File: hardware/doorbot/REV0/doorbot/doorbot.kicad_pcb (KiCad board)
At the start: 2 copper layers, 35 parts, among them J1 Raspberry_Pi_2_3, J2 Screw_Terminal_01x12, J3 PoE, Q1 2N7002, U1 ATmega328P-AU, U2 TLP291, U3 TLP291, U4 TLP291, U5 TLP291, U6 TLP291, U7 DRV103, U8 L78L05_SO8

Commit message: more doorbot schematic & pcb work
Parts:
- added R19: 47, Resistors_SMD:R_0603, B.Cu at (131.4, 71.1)
- added R20: 47, Resistors_SMD:R_0603, B.Cu at (128.3, 71.1)
- added R21: 47, Resistors_SMD:R_0603, B.Cu at (134.6, 71.1)
- added R22: 47, Resistors_SMD:R_0603, B.Cu at (153.0, 71.1)
- C2: footprint C_0201_0603Metric -> Capacitors_SMD:CP_Elec_3x5.3
- J3: value PoE -> PoE Passthrough
- R1, R10, R11, R12, R13, R14, R15, R16, R18, R2, R3, R5, R6, R7, R8, R9: footprint Resistor_SMD:R_0603_1608Metric -> Resistors_SMD:R_0603
- R17: value R_Small_US -> 100; footprint Resistor_SMD:R_0603_1608Metric -> Resistors_SMD:R_0603
- R4: value 10 -> 47; footprint Resistor_SMD:R_0603_1608Metric -> Resistors_SMD:R_0603
- U8: value L78L05_SO8 -> MC78L05_SOT89; footprint Package_SO:SOIC-8_3.9x4.9mm_P1.27mm -> TO_SOT_Packages_SMD:SOT-89-3_Handsoldering
- moved R4 38.8 mm to (117.5, 71.1)
- moved R6 38.7 mm to (114.3, 71.1)
- moved C3 35.7 mm to (164.5, 76.8)
- moved U8 28.6 mm to (165.1, 85.1), turned to 0 degrees
- moved C4 24.3 mm to (164.5, 89.5)
- moved R12 19.4 mm to (135.9, 92.1)
- moved C2 18.5 mm to (164.5, 80.0)
- moved R5 16.1 mm to (139.1, 71.1)
- moved U6 16.0 mm to (132.7, 95.2)
- moved D1 14.4 mm to (149.9, 102.2), turned to 0 degrees
- moved R7 13.8 mm to (152.4, 85.1), turned to 90 degrees
- moved R8 13.1 mm to (154.3, 85.1)
- moved R17 13.0 mm to (132.7, 101.6)
- moved U4 12.7 mm to (123.8, 95.2)
- moved Q1 10.7 mm to (151.1, 88.9), turned to 90 degrees
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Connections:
- net Net-(J2-Pad5) renamed /WG_D0_RAW
- net Net-(J2-Pad6) renamed /WG_D1_RAW
- J1 pad 12: Net-(J1-Pad12) -> /ICSP_MISO
- J1 pad 16: Net-(J1-Pad16) -> /ICSP_MOSI
- J1 pad 18: Net-(J1-Pad18) -> /ICSP_SCK
- J1 pad 32: Net-(J1-Pad32) -> /ICSP_RESET
- R4 pad 2: Net-(J1-Pad33) -> Net-(J1-Pad5)
- R6 pad 2: Net-(J1-Pad32) -> Net-(J1-Pad3)
- U1 pad 15: Net-(U1-Pad15) -> /AT_MOSI
- U1 pad 16: Net-(U1-Pad16) -> /AT_MISO
- U1 pad 17: Net-(U1-Pad17) -> /AT_SCK
- U1 pad 29: Net-(U1-Pad29) -> /AT_RST
- U8 pad 3: Earth -> +12VA
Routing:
- net /WG_D0: track 22.1 -> 0.00 mm, vias 2 -> 0
- net /WG_D1: track 19.7 -> 0.00 mm, vias 2 -> 0
- net Net-(Q1-Pad3): track 0.00 -> 18.2 mm, vias 0 -> 2
- net Net-(U3-Pad2): track 0.00 -> 17.3 mm, vias 0 -> 2
- net +12VA: track 0.00 -> 17.1 mm, vias 0 -> 1
- net /SOLENOID_LOW: track 0.00 -> 11.1 mm, vias 0 -> 1
- net Net-(R13-Pad1): track 0.00 -> 11.1 mm
- net Net-(C1-Pad1): track 0.00 -> 8.79 mm
- net Net-(R14-Pad1): track 0.00 -> 7.15 mm
- net /AT_RXD: track 5.62 -> 0.00 mm
- net /AT_TXD: track 5.35 -> 0.00 mm
- net Net-(Q1-Pad1): track 0.00 -> 4.94 mm
- net Net-(R7-Pad2): track 0.00 -> 4.47 mm
- net +5VA: track 0.00 -> 3.35 mm
- net Net-(R9-Pad2): track 0.00 -> 2.15 mm
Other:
- board text added: "PWR.12V"
- board text added: "PWR.GND"
- board text added: "RFID.12V"
- board text added: "RFID.D0"
- board text added: "RFID.D1"
- board text added: "RFID.GND"
- board text added: "SOL.A"
- board text added: "SOL.B"
- board text added: "SW.A"
- board text added: "SW.B"

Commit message: moar doorbot pcb
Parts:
- added R23: 47, Resistor_SMD:R_0603_1608Metric, B.Cu at (118.9, 91.9)
- R1, R10, R11, R12, R13, R14, R15, R16, R17, R18, R19, R2, R20, R21, R22, R3, R4, R5, R6, R7, R8, R9: footprint Resistors_SMD:R_0603 -> Resistor_SMD:R_0603_1608Metric
- moved R11 17.7 mm to (137.2, 79.5), turned to 180 degrees
- moved R12 10.9 mm to (137.2, 81.2), turned to 180 degrees
- moved R17 0.99 mm to (133.5, 101.0)
- moved R16 0.61 mm to (129.0, 101.0)
- moved R18 0.60 mm to (124.5, 101.0)
- moved R10 0.13 mm to (120.7, 91.9)
- turned R19 to 270 degrees
- turned R20 to 270 degrees
- turned R21 to 270 degrees
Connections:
- R4 pad 2: Net-(J1-Pad5) -> Net-(J1-Pad29)
- R6 pad 2: Net-(J1-Pad3) -> Net-(J1-Pad7)
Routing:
- net +5VA: track 3.35 -> 63.1 mm, vias 0 -> 4
- net +3V3: track 0.00 -> 58.9 mm, vias 0 -> 2
- net +5V: track 0.00 -> 58.2 mm, vias 0 -> 1
- net Net-(J1-Pad31): track 0.00 -> 54.9 mm, vias 0 -> 2
- net Net-(R4-Pad1): track 0.00 -> 54.3 mm, vias 0 -> 4
- net Net-(R6-Pad1): track 0.00 -> 47.7 mm
- net Net-(J1-Pad29): track 0.00 -> 46.8 mm, vias 0 -> 3
- net +12VA: track 17.1 -> 58.7 mm, vias 1 -> 5
- net /AT_RST: track 0.00 -> 37.2 mm, vias 0 -> 2
- net /WG_D0: track 0.00 -> 30.6 mm, vias 0 -> 2
- net /AT_MOSI: track 0.00 -> 25.2 mm, vias 0 -> 2
- net /AT_SCK: track 0.00 -> 23.1 mm, vias 0 -> 2
- net /AT_MISO: track 0.00 -> 20.9 mm, vias 0 -> 2
- net Earth: track 0.00 -> 17.0 mm, vias 0 -> 6
- net /WG_D1: track 0.00 -> 17.0 mm, vias 0 -> 2
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- added copper zone on B.Cu, net Earth
- added copper zone on B.Cu, net GND
- added copper zone on F.Cu, net GND

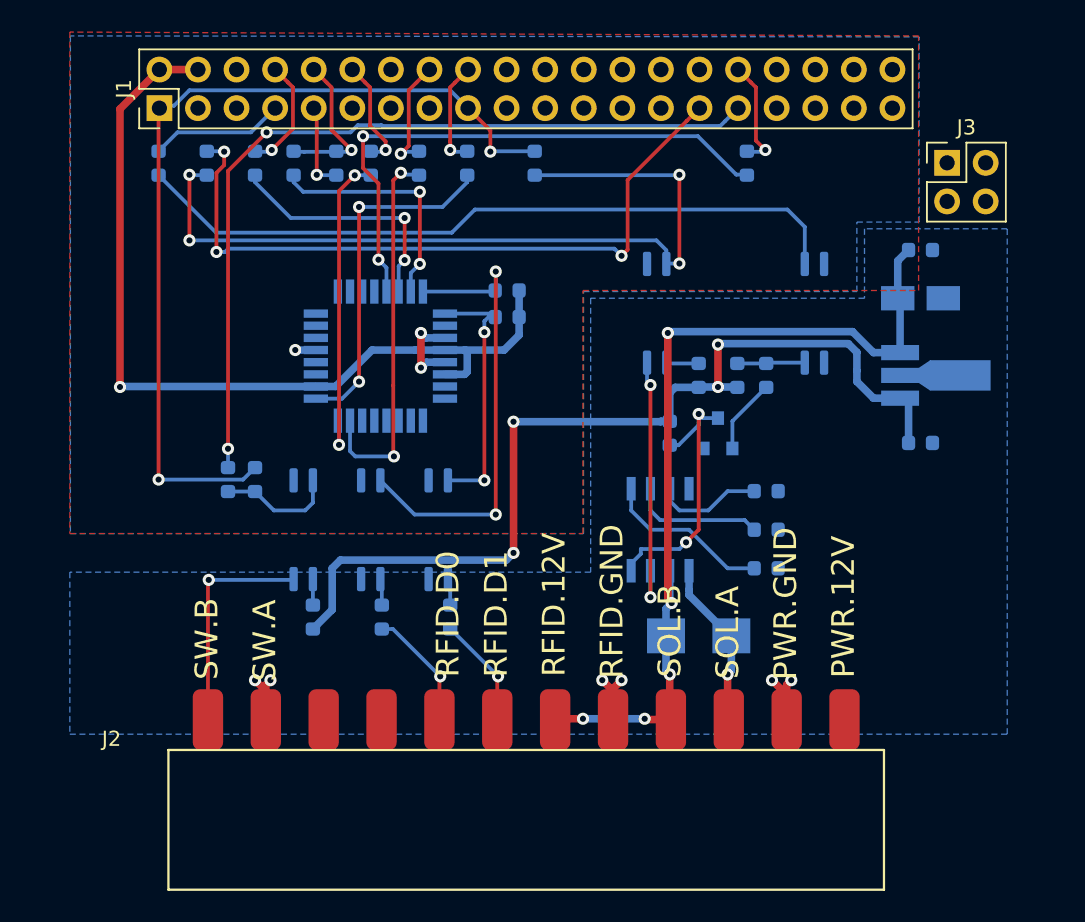
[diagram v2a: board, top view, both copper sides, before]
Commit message: doorbot: add dc boost for 24v option, PTC fuse
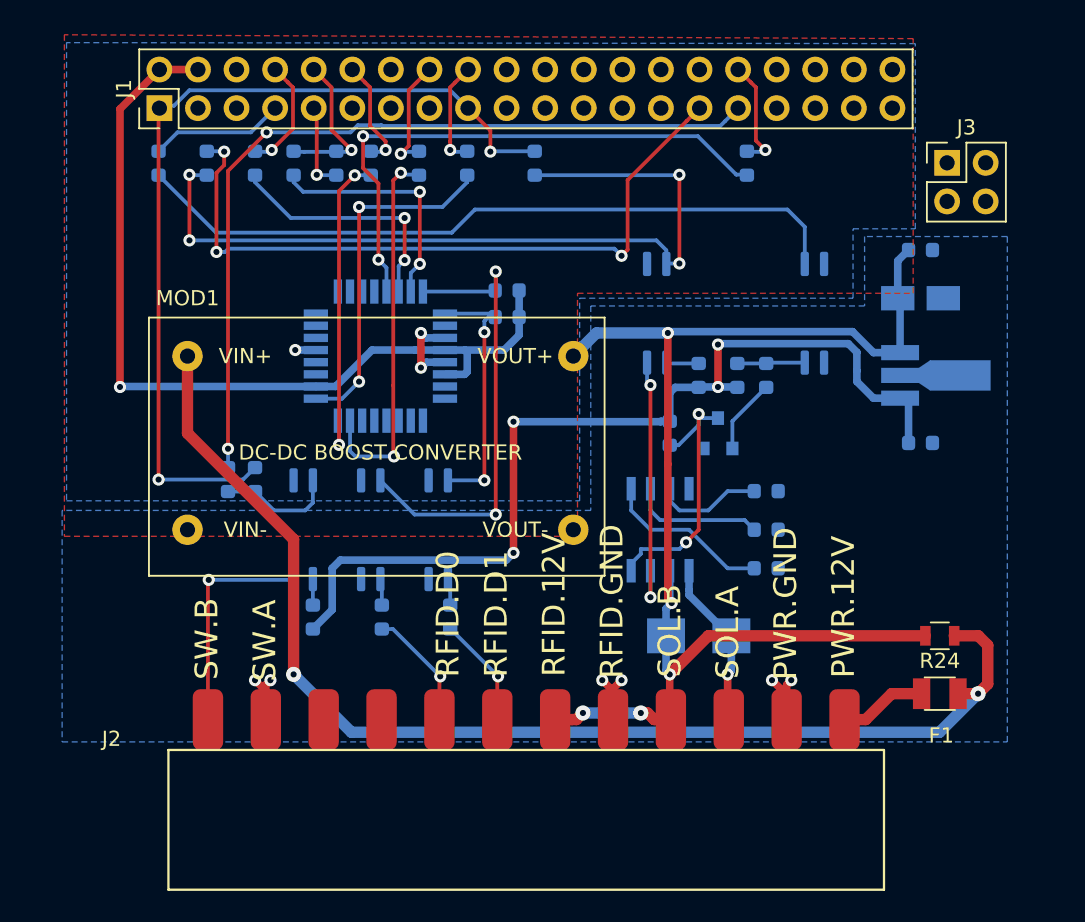
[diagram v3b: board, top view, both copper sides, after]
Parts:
- added F1: 1.5A PTC, Fuse_Holders_and_Fuses:Fuse_SMD1206_Reflow, F.Cu at (165.7, 106.0)
- added MOD1: DC_BOOST_MODULE, doorbot_pcb_library:DC_BOOST_MODULE, F.Cu at (113.7, 81.3)
- added R24: 0, Resistors_SMD:R_0805, F.Cu at (165.7, 102.2)
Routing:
- net Net-(F1-Pad1): track 0.00 -> 78.9 mm, vias 0 -> 2
- net +12VA: track 58.7 -> 83.8 mm
- net /+12V_IN: track 0.00 -> 5.78 mm

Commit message: more doorbot schematic & pcb, routed and passes drc but not complete
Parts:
- added C5: .1uF, Capacitor_SMD:C_0603_1608Metric, B.Cu at (135.6, 84.3)
- added C6: .1uF, Capacitor_SMD:C_0603_1608Metric, B.Cu at (121.9, 85.1)
- added REF**: MountingHole_2.7mm_M2.5_ISO14580, MountingHole:MountingHole_2.7mm_M2.5_ISO14580, F.Cu at (128.0, 117.1)
- added REF**: MountingHole_2.7mm_M2.5_ISO14580, MountingHole:MountingHole_2.7mm_M2.5_ISO14580, F.Cu at (182.9, 114.8)
- added REF**: MountingHole_2.7mm_M2.5_ISO14580, MountingHole:MountingHole_2.7mm_M2.5_ISO14580, F.Cu at (108.7, 63.5)
- added REF**: MountingHole_2.7mm_M2.5_ISO14580, MountingHole:MountingHole_2.7mm_M2.5_ISO14580, F.Cu at (176.5, 65.5)
- moved C2 31.1 mm to (140.7, 100.1), turned to 180 degrees
- moved C3 4.19 mm to (164.6, 81.0)
- moved R18 0.60 mm to (124.5, 101.6)
- moved R16 0.57 mm to (129.0, 101.6)
- moved R17 0.57 mm to (133.5, 101.6)
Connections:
- C2 pad 1: +12VA -> +VSW
- D1 pad 1: +12VA -> +VSW
- F1 pad 1: Net-(F1-Pad1) -> +12VA
- J2 pad 9: +12VA -> +VSW
- MOD1 pad 1: Net-(F1-Pad1) -> +12VA
- MOD1 pad 3: +12VA -> +VSW
- R24 pad 1: Net-(F1-Pad1) -> +12VA
- R24 pad 2: +12VA -> +VSW
- U7 pad 6: +12VA -> +VSW
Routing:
- net Net-(F1-Pad1): track 78.9 -> 0.00 mm, vias 2 -> 0
- net +VSW: track 0.00 -> 52.3 mm, vias 0 -> 2
- net GND: track 12.9 -> 51.1 mm, vias 4 -> 5
- net +12VA: track 83.8 -> 112.5 mm, vias 5 -> 4
- net +5V: track 58.2 -> 52.4 mm
- net /DOOR_SWITCH_IN: track 14.8 -> 12.5 mm
- net /AT_RST: track 37.2 -> 38.2 mm
- net /PI_RXD: track 10.2 -> 11.0 mm
- net Net-(R18-Pad1): track 1.75 -> 2.31 mm
- net Net-(R16-Pad2): track 1.79 -> 2.33 mm
- net Net-(R17-Pad2): track 1.81 -> 2.35 mm
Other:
- board text added: "R.12V"
- board text added: "R.D0"
- board text added: "R.D1"
- board text added: "R.GND"
- board text removed: "RFID.12V"
- board text removed: "RFID.D0"
- board text removed: "RFID.D1"
- board text removed: "RFID.GND"

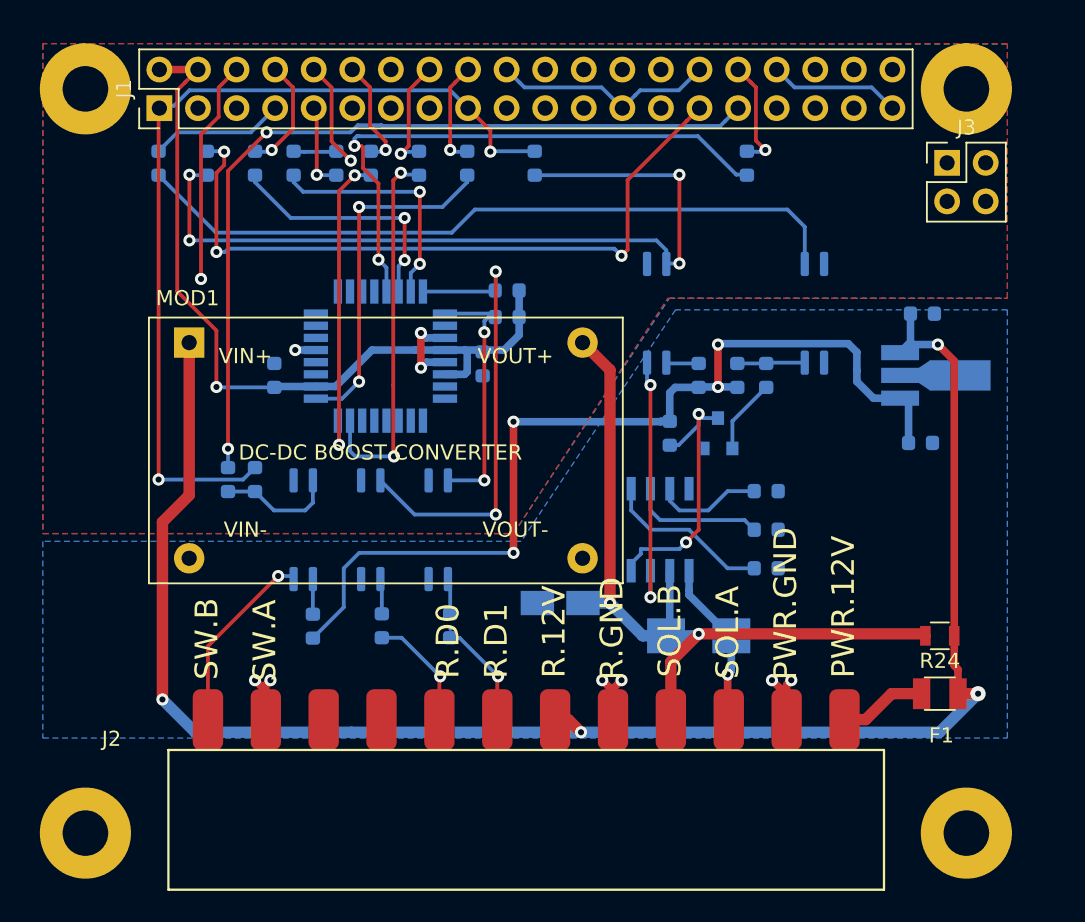
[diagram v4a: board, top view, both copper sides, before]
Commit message: add a couple 3d models
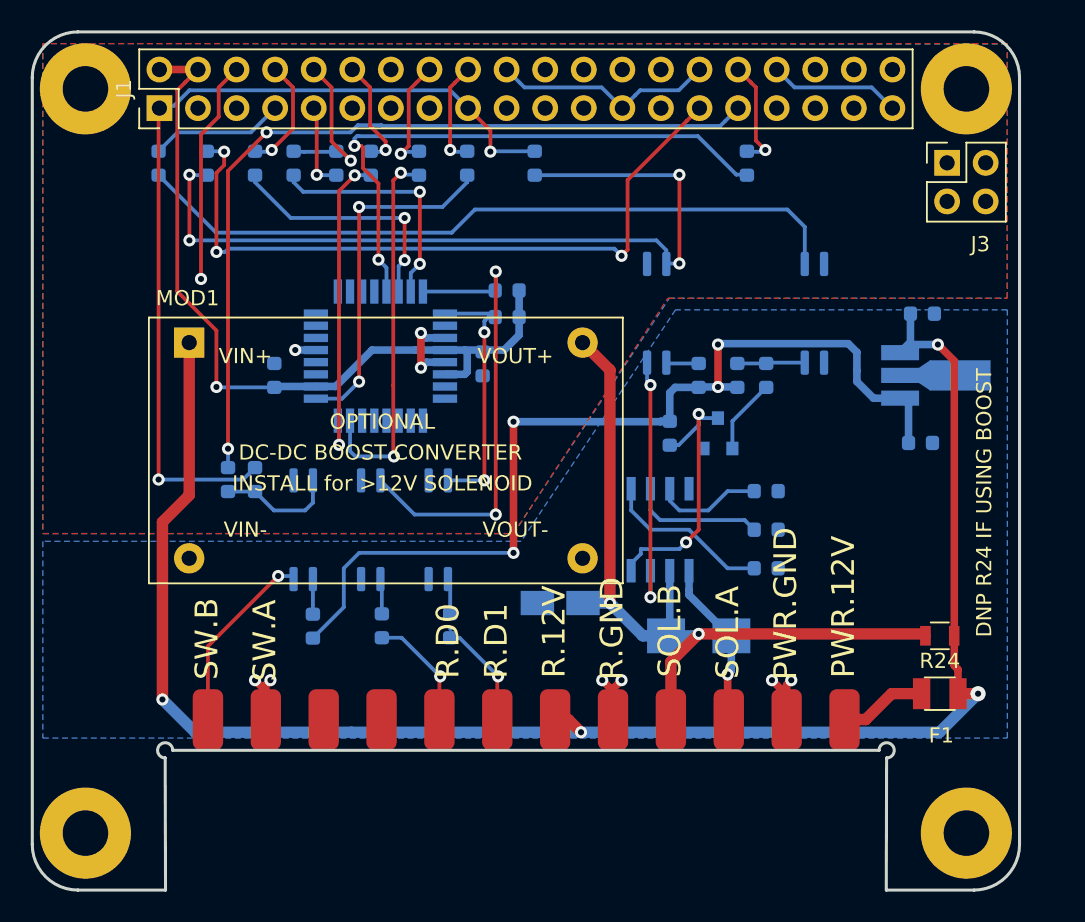
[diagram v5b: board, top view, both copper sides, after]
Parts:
- J1: footprint Connector_PinHeader_2.54mm:PinHeader_2x20_P2.54mm_Vertical -> doorbot_pcb_library:PinHeader_2x20_P2.54mm_Vertical
- J3: footprint Connector_PinHeader_2.54mm:PinHeader_2x02_P2.54mm_Vertical -> doorbot_pcb_library:PinHeader_2x02_P2.54mm_Vertical
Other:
- board outline added: 65 x 56.5 mm
- board text added: "DNP R24 IF USING BOOST"
- board text added: "INSTALL for >12V SOLENOID"
- board text added: "OPTIONAL"

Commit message: add wiegand led/buzzer control, leds, some rerouting
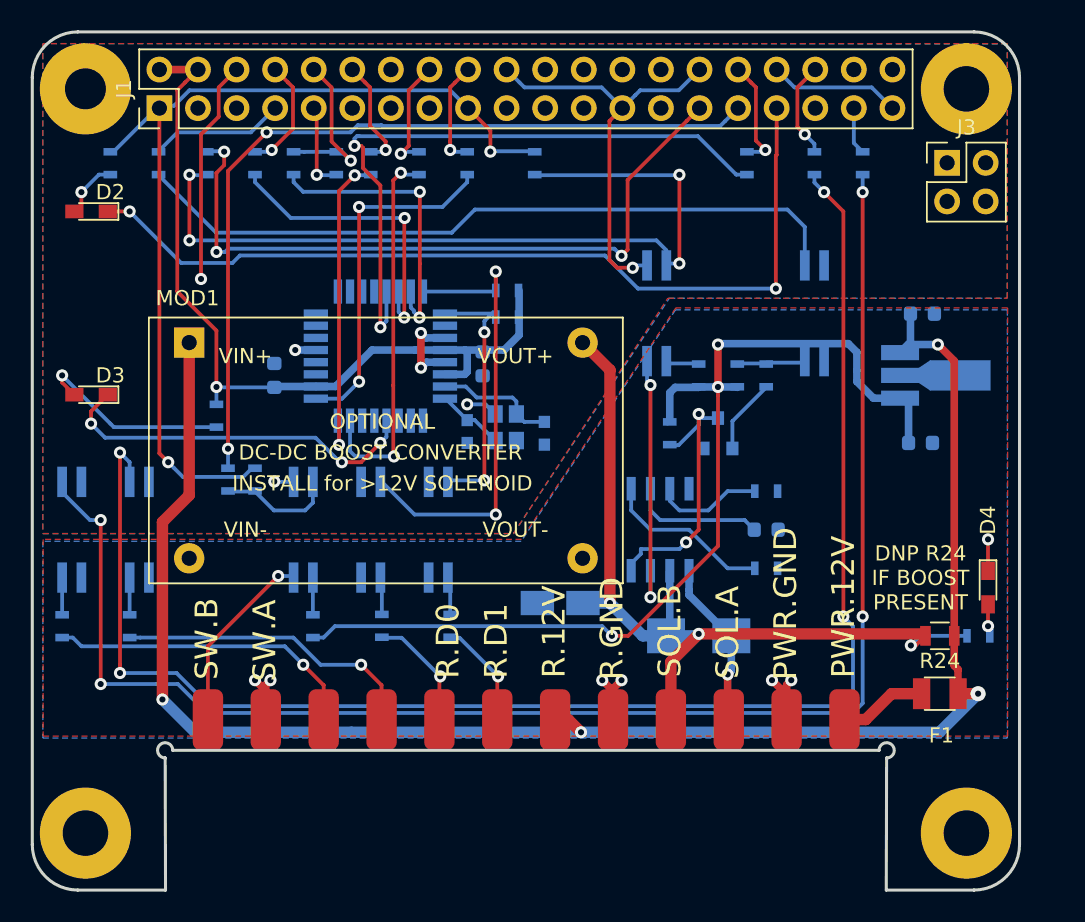
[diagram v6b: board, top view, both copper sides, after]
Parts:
- removed REF** (x4): MountingHole_2.7mm_M2.5_ISO14580, MountingHole:MountingHole_2.7mm_M2.5_ISO14580
- added C7: 12pF, Capacitors_SMD:C_0603, B.Cu at (134.6, 88.8)
- added C8: 12pF, Capacitors_SMD:C_0603, B.Cu at (139.7, 88.9)
- added D2: LED, LEDs:LED_0603_HandSoldering, F.Cu at (109.9, 74.3)
- added D3: LED, LEDs:LED_0603_HandSoldering, F.Cu at (109.9, 86.4)
- added D4: LED, LEDs:LED_0603_HandSoldering, F.Cu at (168.9, 99.1)
- added H1: MountingHole, Mounting_Holes:MountingHole_2.7mm_M2.5, F.Cu at (101.0, 66.2)
- added H2: MountingHole, Mounting_Holes:MountingHole_2.7mm_M2.5, F.Cu at (103.5, 118.1)
- added H3: MountingHole, Mounting_Holes:MountingHole_2.7mm_M2.5, F.Cu at (173.4, 61.6)
- added H4: MountingHole, Mounting_Holes:MountingHole_2.7mm_M2.5, F.Cu at (174.0, 117.5)
- added R25: 100, Resistors_SMD:R_0603, B.Cu at (160.7, 71.1)
- added R26: 100, Resistors_SMD:R_0603, B.Cu at (157.5, 71.1)
- added R27: 47, Resistors_SMD:R_0603, B.Cu at (108.0, 101.6)
- added R28: 47, Resistors_SMD:R_0603, B.Cu at (112.4, 101.6)
- added R29: 100, Resistors_SMD:R_0603, B.Cu at (111.1, 71.1)
- added R30: 100, Resistors_SMD:R_0603, B.Cu at (118.1, 87.7)
- added R31: 1K, Resistors_SMD:R_0603, B.Cu at (168.3, 102.2)
- added U10: TLP291, Housings_SOIC:SO-4_4.4x2.3mm_Pitch1.27mm, B.Cu at (113.0, 95.2)
- added U9: TLP291, Housings_SOIC:SO-4_4.4x2.3mm_Pitch1.27mm, B.Cu at (108.6, 95.2)
- added Y1: 16MHz, Crystals:Crystal_SMD_2520-4pin_2.5x2.0mm, B.Cu at (137.2, 88.5)
- J1: footprint doorbot_pcb_library:PinHeader_2x20_P2.54mm_Vertical -> Pin_Headers:Pin_Header_Straight_2x20_Pitch2.54mm
- J3: footprint doorbot_pcb_library:PinHeader_2x02_P2.54mm_Vertical -> Pin_Headers:Pin_Header_Straight_2x02_Pitch2.54mm
- R1, R10, R11, R12, R13, R14, R15, R16, R17, R18, R19, R2, R20, R21, R22, R23, R3, R4, R5, R6, R7, R8, R9: footprint Resistor_SMD:R_0603_1608Metric -> Resistors_SMD:R_0603
- U2, U3, U4, U5, U6: footprint Package_SO:SOIC-4_4.55x2.6mm_P1.27mm -> Housings_SOIC:SO-4_4.4x2.3mm_Pitch1.27mm
- U7: footprint Package_SO:SOIC-8_3.9x4.9mm_P1.27mm -> Housings_SOIC:SOIC-8_3.9x4.9mm_Pitch1.27mm
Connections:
- net /ICSP_MISO renamed ICSP_MISO
- net /ICSP_MOSI renamed ICSP_MOSI
- net /ICSP_RESET renamed ICSP_RESET
- net /ICSP_SCK renamed ICSP_SCK
- net /PI_RXD renamed PI_RXD
- net /PI_TXD renamed PI_TXD
- net /WG_D0 renamed WG_D0
- net /WG_D1 renamed WG_D1
- net Net-(J1-Pad29) renamed SOL_OK
- net Net-(J1-Pad31) renamed DOOR_SW
- net Net-(J1-Pad7) renamed SOL_ENABLE
- J1 pad 36: Net-(J1-Pad36) -> WG_LED
- J1 pad 37: Net-(J1-Pad37) -> WG_BEEP
- J2 pad 3: Net-(J2-Pad3) -> /WG_BEEP_RAW
- J2 pad 4: Net-(J2-Pad4) -> /WG_LED_RAW
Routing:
- net Net-(R26-Pad1): track 0.00 -> 101.4 mm, vias 0 -> 4
- net Net-(R25-Pad1): track 0.00 -> 100.8 mm, vias 0 -> 4
- net Net-(D2-Pad1): track 0.00 -> 58.4 mm, vias 0 -> 2
- net Net-(D3-Pad1): track 0.00 -> 24.6 mm, vias 0 -> 3
- net /WG_BEEP_RAW: track 0.00 -> 20.8 mm, vias 0 -> 1
- net /WG_LED_RAW: track 0.00 -> 20.1 mm, vias 0 -> 1
- net GND: track 51.1 -> 67.6 mm, vias 5 -> 8
- net Net-(D3-Pad2): track 0.00 -> 13.2 mm, vias 0 -> 1
- net Net-(C8-Pad1): track 0.00 -> 7.99 mm
- net WG_LED: track 0.00 -> 6.37 mm, vias 0 -> 1
- net +VSW: track 52.3 -> 57.5 mm, vias 2 -> 3
- net /AT_RST: track 38.2 -> 42.8 mm
- net Net-(C7-Pad1): track 0.00 -> 4.45 mm
- net +5VA: track 63.2 -> 67.7 mm, vias 4 -> 3
- net Net-(D2-Pad2): track 0.00 -> 3.85 mm, vias 0 -> 1
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- added copper zone on F.Cu, net Earth
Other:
- board text added: "DNP R24 IF BOOST PRESENT"
- board text removed: "DNP R24 IF USING BOOST"
